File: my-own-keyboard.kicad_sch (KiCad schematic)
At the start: 140 parts, among them J2 5077CR-16SMC2-BK-TR, SW1 Reset SW, SW10 8, SW11 9, SW12 0, SW13 -, SW14 =, SW15 Backspace, SW16 Tab, SW17 Q, SW18 W, SW19 E, SW2 `, SW20 R, SW21 T, SW22 Y, SW23 U, SW24 I, SW25 O, SW26 P, SW27 [, SW28 ], SW29 \, SW3 1, SW30 Capslock, SW31 A, SW32 S, SW33 D, SW34 F, SW35 G, SW36 H, SW37 J, SW38 K, SW39 L, SW4 2, SW40 ;, SW41 ', SW42 Enter, SW43 L-shift, SW44 Z, SW45 X, SW46 C, SW47 V, SW48 B, SW49 N, SW5 3, SW50 M, SW51 ,, SW52 ., SW53 /, SW54 R-shift, SW55 L-Ctrl, SW56 win, SW57 L-Alt, SW58 Space, SW59 Fn, SW6 4, SW60 R-Alt, SW61 Menu, SW62 R-Ctrl, SW63 RotaryEncoder_Switch, SW7 5, SW8 6, SW9 7, U1 ATmega32U4-A, Y1 16MHz

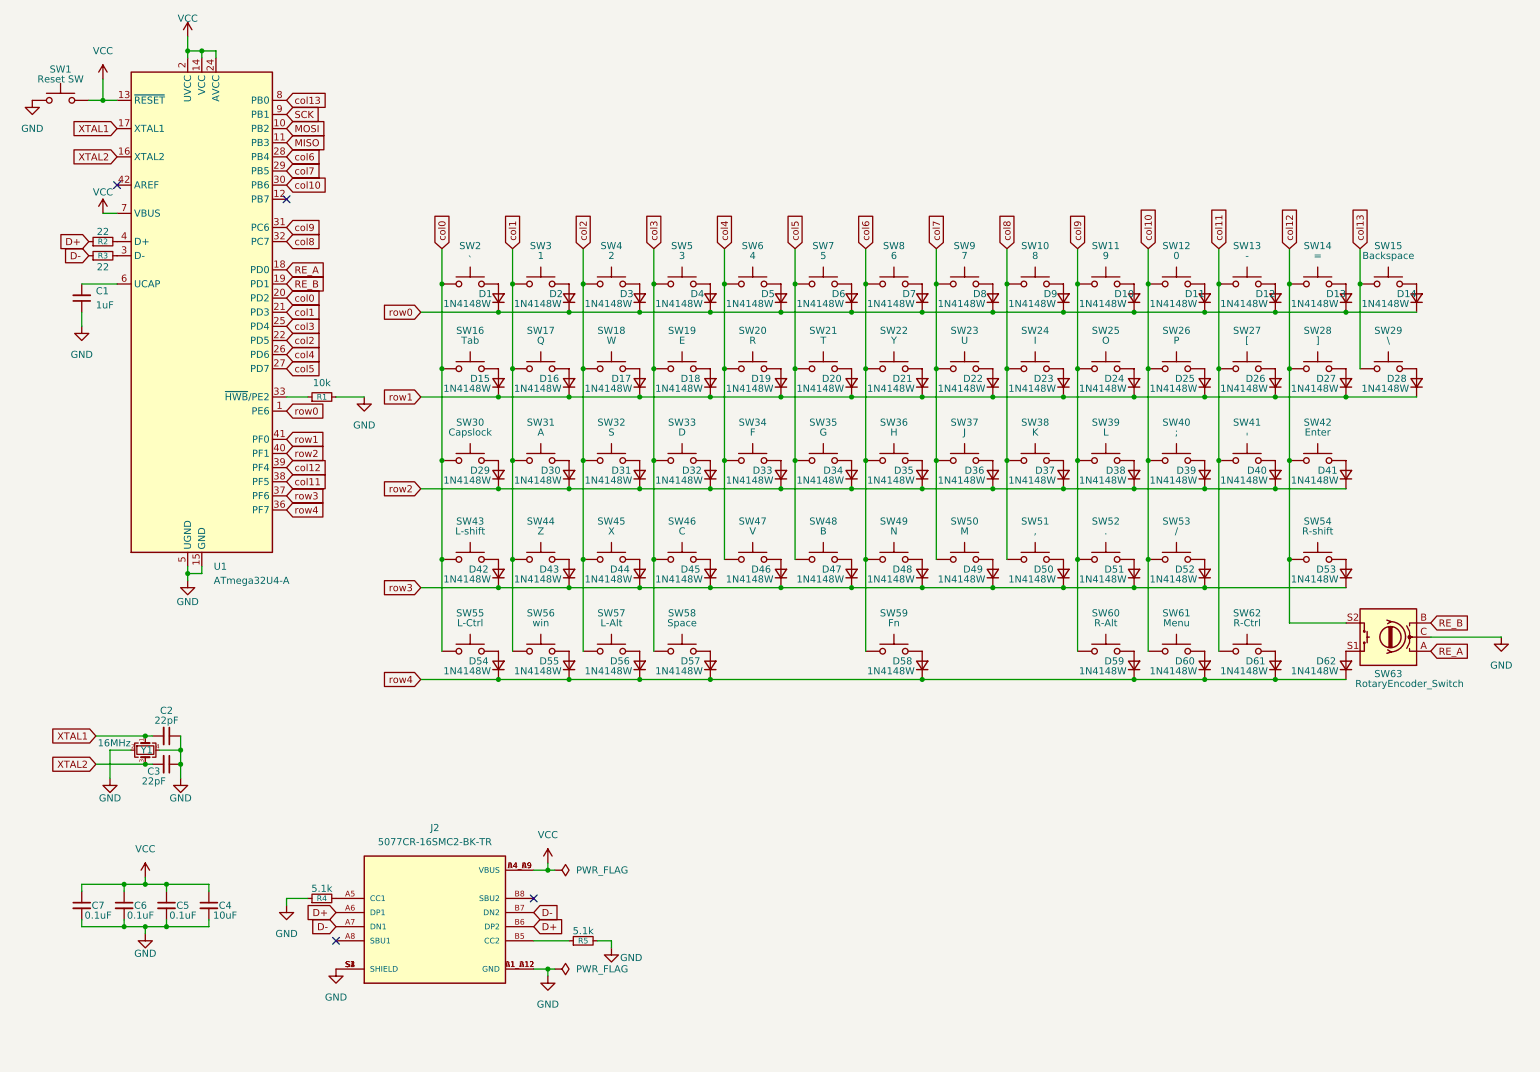
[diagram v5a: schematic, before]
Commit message: added ICSP
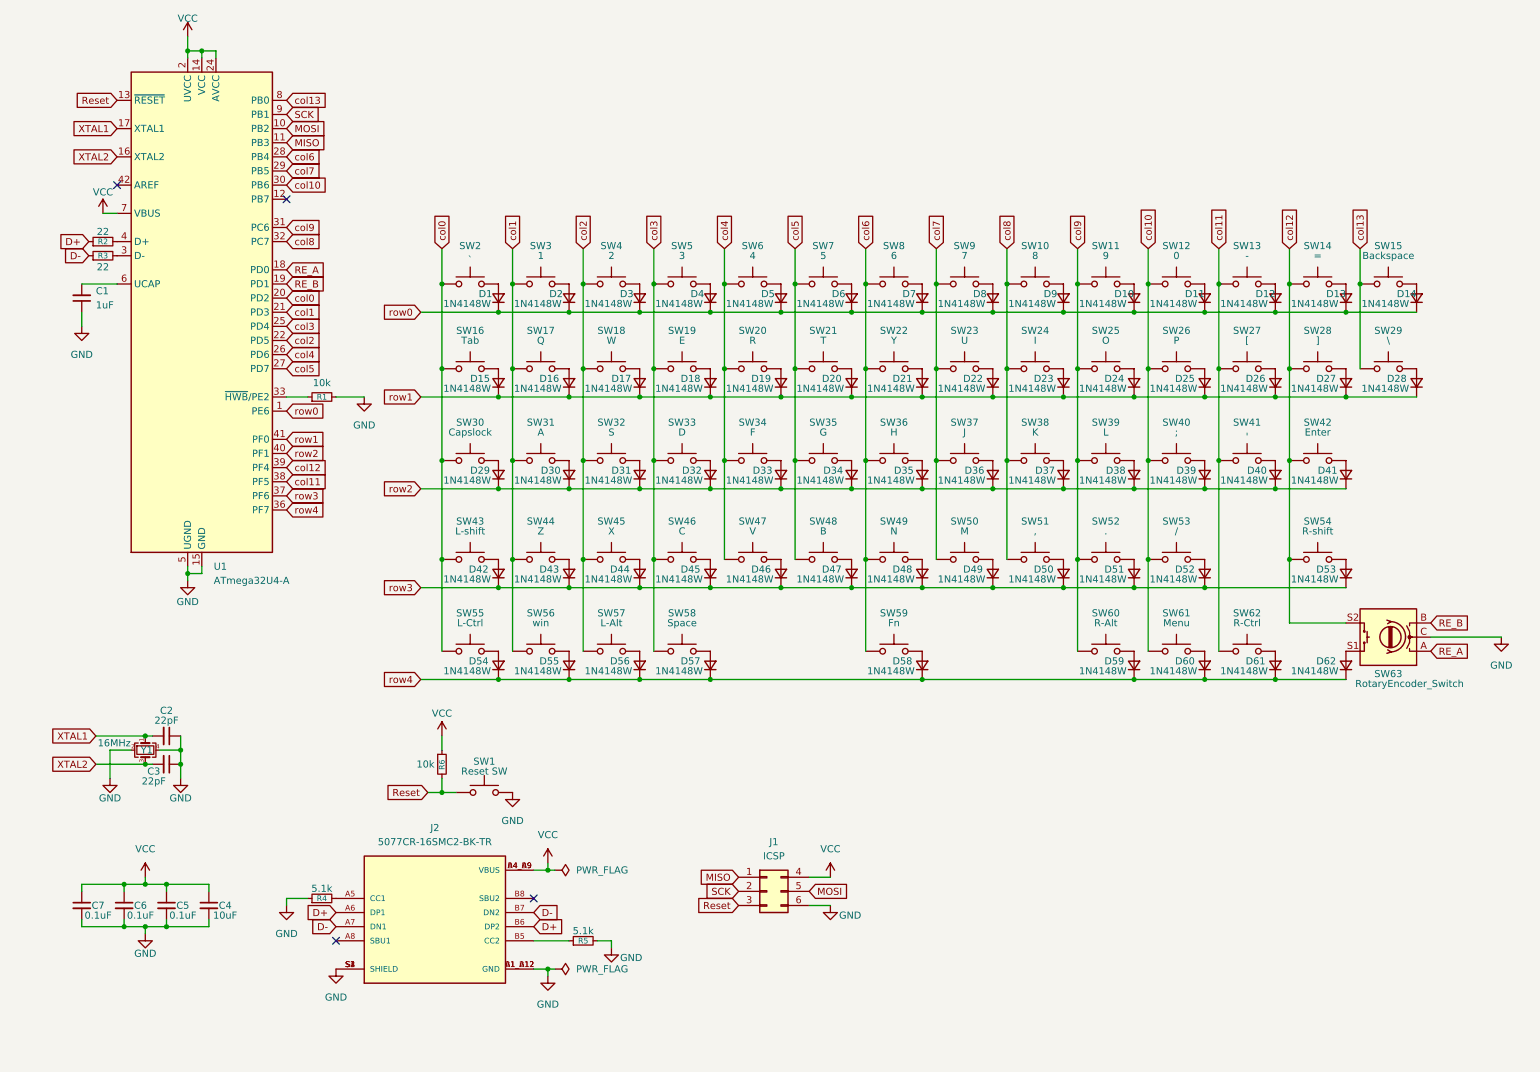
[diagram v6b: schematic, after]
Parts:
- added J1: ICSP, symbol Connector_Generic:Conn_02x03_Top_Bottom
- added R6: 10k, Resistor_SMD:R_0603_1608Metric, symbol Device:R_Small
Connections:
- net GND: now also SW1.2, J1.6 (Pin_6); no longer SW1.1
- net MISO: now also J1.1 (Pin_1)
- net MOSI: now also J1.5 (Pin_5)
- net SCK: now also J1.2 (Pin_2)
- net VCC: now also J1.4 (Pin_4), R6.1; no longer SW1.2, U1.13 (~{RESET})
- new net Reset: J1.3 (Pin_3), R6.2, SW1.1, U1.13 (~{RESET})
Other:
- moved on the sheet: SW1

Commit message: completed all of the design of the PCB
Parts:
- J1: footprint (none) -> Connector_PinSocket_1.27mm:PinSocket_2x03_P1.27mm_Vertical
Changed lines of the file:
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@@
 			)
 		)
-		(property "Footprint" ""
+		(property "Footprint" "Connector_PinSocket_1.27mm:PinSocket_2x03_P1.27mm_Vertical"
 			(at 147.32 170.18 0)
 			(effects

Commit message: updated the pcb
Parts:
- SW1: footprint kbd:ResetSW -> original_library:ResetSW TSHA-T-2.5B2-19SH
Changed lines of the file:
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@@
 			)
 		)
-		(property "Footprint" "kbd:ResetSW"
+		(property "Footprint" "original_library:ResetSW TSHA-T-2.5B2-19SH"
 			(at 96.52 147.32 0)
 			(effects
